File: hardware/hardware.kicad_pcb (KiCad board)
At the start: 2 copper layers, 100 x 100 mm, 17 parts, among them J1 USB_C_Receptacle_USB2.0_14P, J2 Conn_01x04_Socket, J3 Conn_01x08_Socket, J4 Conn_01x04_Socket, J6 Conn_01x05_Socket, U1 AMS1117-3.3, U2 ESP32-S3-WROOM-1

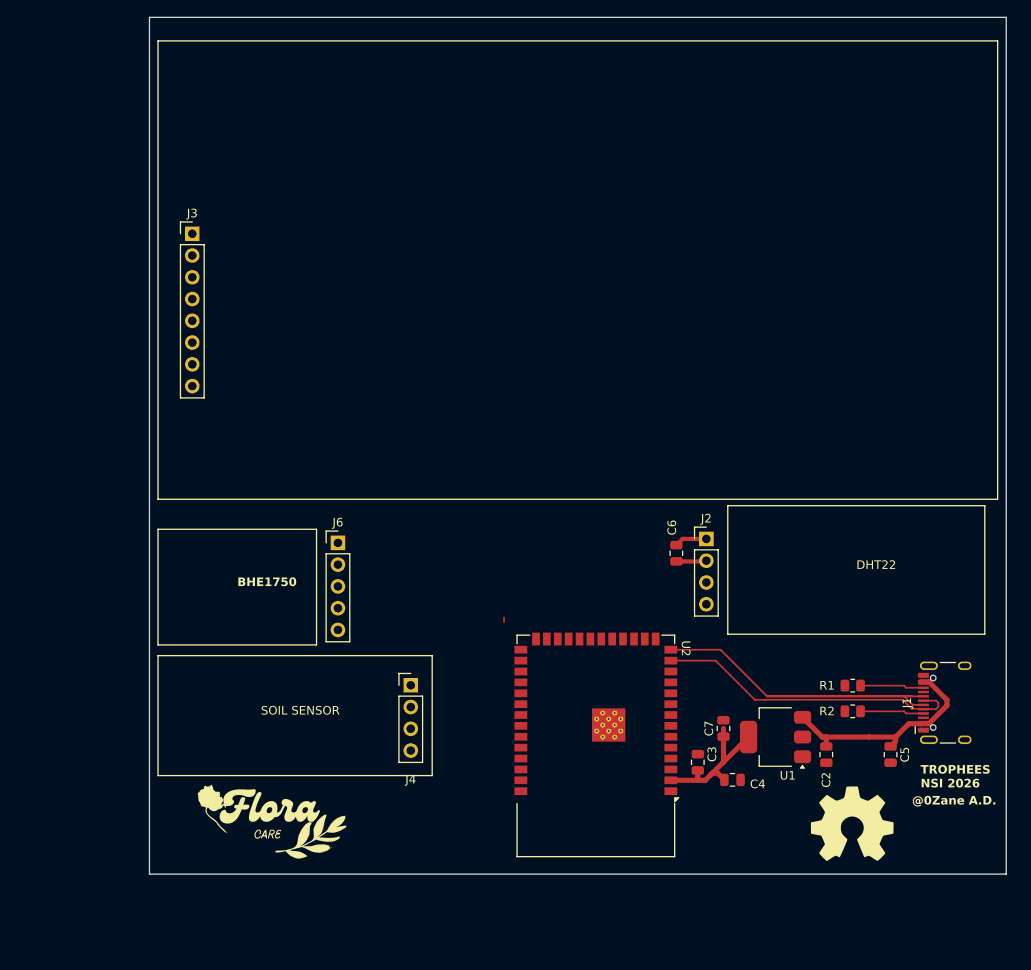
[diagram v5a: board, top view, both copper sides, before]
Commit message: Putting ground over the back of the PCB
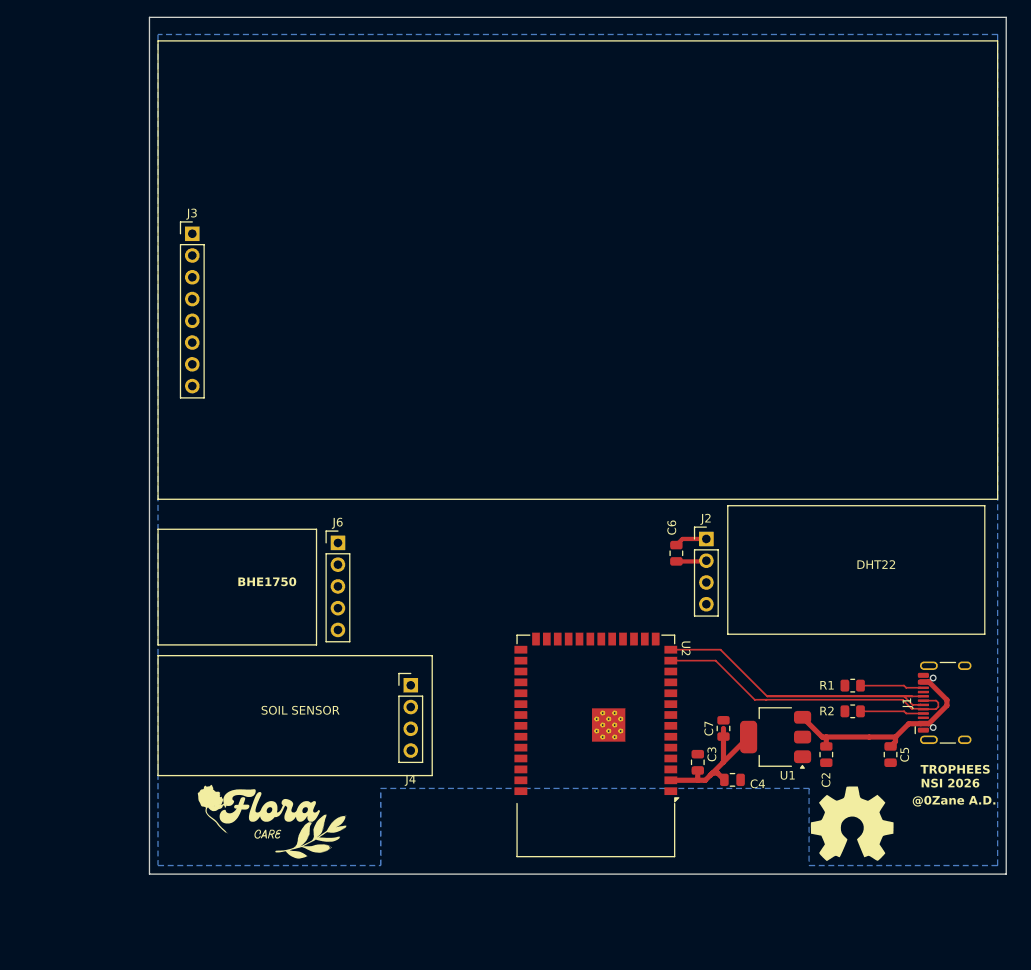
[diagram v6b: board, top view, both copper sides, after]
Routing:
- net DC: track 0.53 -> 0.00 mm
- added copper zone on B.Cu, net GND
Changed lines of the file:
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@@
 		(net 8)
 	)
-	(segment
-		(start 181.805 96.41)
-		(end 181.805 95.878)
-		(width 0.2)
-		(layer "F.Cu")
-		(net 9)
+	(zone
+		(net 2)
+		(net_name "GND")
+		(layer "B.Cu")
+		(hatch edge 0.5)
+		(connect_pads
+			(clearance 0.5)
+		)
+		(min_thickness 0.25)
+		(filled_areas_thickness no)
+		(fill yes
+			(thermal_gap 0.5)
+			(thermal_bridge_width 0.5)
+		)
+		(polygon
+			(pts
+				(xy 141.42 124.85) (xy 167.42 124.85) (xy 167.42 115.85) (xy 217.42 115.85) (xy 217.42 124.85) (xy 239.42 124.85)
+				(xy 239.42 27.85) (xy 141.42 27.85)
+			)
+		)
 	)
 	(embedded_fonts no)
